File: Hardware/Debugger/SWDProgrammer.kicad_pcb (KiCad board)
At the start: 4 copper layers, 21.1 x 14 mm, 32 parts, among them J1 USB_C_Receptacle_USB2.0, U1 AP2112K-3.3, U2 STM32F103C8Tx, Y1 32.768KHZ, Y2 Crystal_GND24_Small

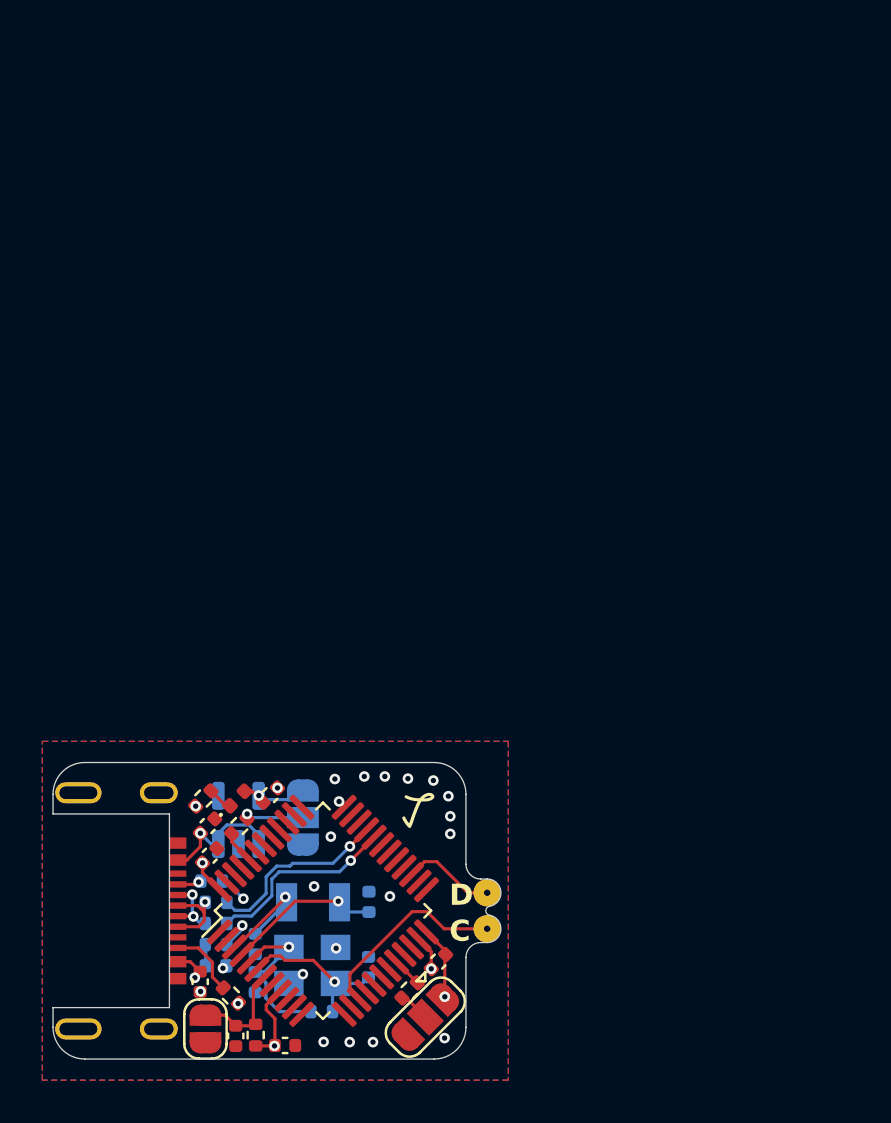
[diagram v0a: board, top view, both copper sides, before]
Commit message: worked on debugger, has to be flipped
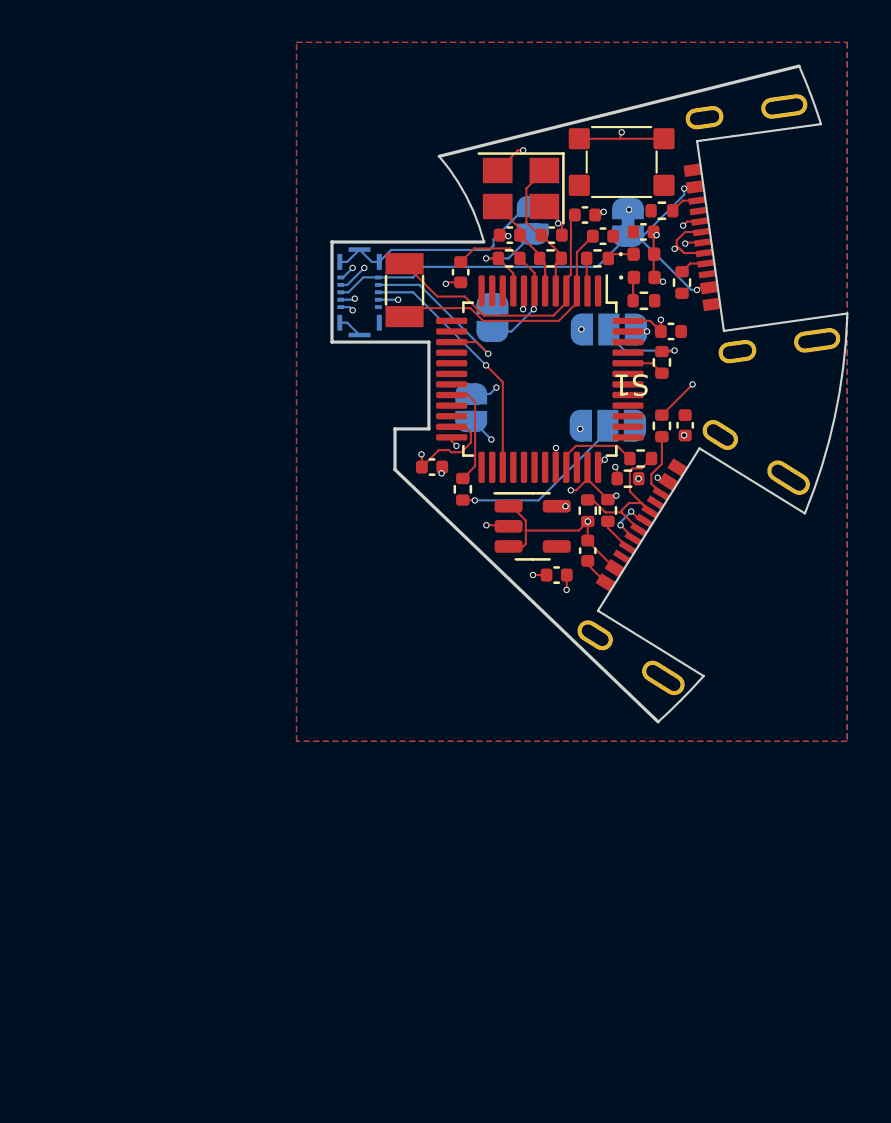
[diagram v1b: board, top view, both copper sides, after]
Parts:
- removed the JP1 at (126.7, 94.6)
- removed P1: ~, Library:Programmer Pin
- added J2: USB_C_Receptacle_USB2.0, Library:USB-C_C168688, F.Cu at (150.5, 57.2)
- added JP1: SolderJumper_2_Open, Jumper:SolderJumper-2_P1.3mm_Open_RoundedPad1.0x1.5mm, B.Cu at (140.2, 61.0)
- added JP1: SolderJumper_2_Open, Jumper:SolderJumper-2_P1.3mm_Open_RoundedPad1.0x1.5mm, B.Cu at (139.2, 65.2)
- added JP4: Jumper_2_Open, Jumper:SolderJumper-2_P1.3mm_Open_RoundedPad1.0x1.5mm, B.Cu at (142.2, 56.4)
- added JP5: Jumper_2_Bridged, Jumper:SolderJumper-2_P1.3mm_Bridged_RoundedPad1.0x1.5mm, B.Cu at (146.7, 56.5)
- added R11: 1.5K, Resistor_SMD:R_0402_1005Metric, F.Cu at (144.8, 70.1)
- added R12: 5.1K, Resistor_SMD:R_0402_1005Metric, F.Cu at (148.2, 56.0)
- added R13: 5.1K, Resistor_SMD:R_0402_1005Metric, F.Cu at (149.2, 59.3)
- added S1: Button, Library:button 3x3, F.Cu at (146.3, 53.6)
- added U3: ~, Library:BK13C06-10DS, B.Cu at (134.0, 59.8)
- C10, C11, C3, C4, D1, R10, R3, R5, R6, R7, U1, Y1: moved to F.Cu
- JP3: moved to B.Cu
- Y2: value Crystal_GND24_Small -> 8Mhz; moved to F.Cu
- moved D1 39.2 mm to (147.4, 58.0)
- moved R4 38.6 mm to (141.0, 58.2), turned to 0 degrees
- moved Y2 38.0 mm to (141.6, 54.9), turned to 180 degrees
- moved C11 37.9 mm to (143.1, 57.1), turned to 180 degrees
- moved C5 37.6 mm to (138.8, 58.9)
- moved C3 37.2 mm to (145.5, 57.1), turned to 180 degrees
- moved R7 37.2 mm to (143.0, 58.2), turned to 0 degrees
- moved R3 37.1 mm to (145.2, 58.2), turned to 180 degrees
- moved C7 35.9 mm to (147.4, 57.0), turned to 0 degrees
- moved C10 35.2 mm to (141.1, 57.1), turned to 0 degrees
- moved C4 34.0 mm to (144.6, 56.1), turned to 0 degrees
- moved R9 33.7 mm to (148.2, 66.1), turned to -90 degrees
- moved R8 31.4 mm to (147.4, 60.2), turned to 0 degrees
- moved D2 31.2 mm to (147.4, 59.1), turned to 0 degrees
- moved R1 29.6 mm to (148.2, 63.1), turned to -90 degrees
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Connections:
- J1 pad S2: unconnected-(J1-SHIELD-PadS1) -> unconnected-(J1-SHIELD-PadS2)
- J1 pad S3: unconnected-(J1-SHIELD-PadS1) -> unconnected-(J1-SHIELD-PadS3)
- J1 pad S4: unconnected-(J1-SHIELD-PadS1) -> unconnected-(J1-SHIELD-PadS4)
- U2 pad 15: /A5 -> swc
- U2 pad 27: /B14 -> swd
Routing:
- net 5V(2): track 0.00 -> 23.9 mm, vias 0 -> 2
- net D-: track 0.00 -> 20.7 mm, vias 0 -> 2
- net D+: track 0.00 -> 20.6 mm, vias 0 -> 3
- net RESET: track 0.00 -> 20.5 mm, vias 0 -> 2
- net GND: track 2.96 -> 21.6 mm, vias 23 -> 13
- net SDA: track 0.00 -> 14.1 mm, vias 0 -> 2
- net 5V: track 15.4 -> 28.8 mm, vias 2 -> 4
- net SCL: track 0.00 -> 12.6 mm, vias 0 -> 2
- net swd: track 0.00 -> 11.7 mm, vias 0 -> 1
- net VDD_nRF: track 0.00 -> 10.8 mm
- net /A5: track 9.42 -> 0.00 mm
- net swc: track 0.00 -> 8.49 mm, vias 0 -> 1
- net unconnected-(J1-SHIELD-PadS1): track 7.60 -> 0.00 mm
- net /BOOT1: track 1.47 -> 8.46 mm, vias 0 -> 1
- net Net-(U2-PC14): track 5.51 -> 12.4 mm, vias 1 -> 0
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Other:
- board size 21.1 x 14 mm -> 24.3 x 31 mm
- board text added: "3V"
- board text added: "5V"
- board text added: "BOOT0"
- board text added: "BOOT1"
- board text added: "PASS TO"
- board text added: "RST"
- board text added: "SCL"
- board text added: "SDA"
- board text removed: "Tongtong.inc"

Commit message: finished debugger and wireless
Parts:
- added JP7: SolderJumper_2_Open, Jumper:SolderJumper-2_P1.3mm_Open_RoundedPad1.0x1.5mm, F.Cu at (141.2, 62.5)
- added JP7: SolderJumper_2_Open, Jumper:SolderJumper-2_P1.3mm_Open_RoundedPad1.0x1.5mm, F.Cu at (141.2, 59.7)
- C1, C10, C11, C2, C3, C4, C5, C6, C7, C8, C9, D1, D2, J1, J2, R1, R10, R11, R12, R13, R2, R3, R4, R5, R6, R7, R8, R9, S1, U1, U2, Y1, Y2: moved to B.Cu
- JP1, JP2, JP3, JP4, JP5, U3: moved to F.Cu
- JP7: renamed from JP1; moved to F.Cu
- moved C8 12.2 mm to (138.7, 68.6), turned to 90 degrees
- moved C9 11.1 mm to (148.3, 66.2), turned to -90 degrees
- moved R2 10.9 mm to (148.8, 64.5), turned to 180 degrees
- moved R4 10.4 mm to (137.6, 68.0), turned to 90 degrees
- moved Y1 10.2 mm to (145.8, 56.6), turned to 0 degrees
- moved C7 10.1 mm to (137.8, 60.2)
- moved D1 9.79 mm to (137.7, 58.9), turned to -90 degrees
- moved JP1 8.23 mm to (140.9, 69.2), turned to 0 degrees
- moved R9 6.93 mm to (144.7, 72.1)
- moved R3 6.59 mm to (138.7, 58.9), turned to -90 degrees
- moved C6 4.76 mm to (139.6, 70.1), turned to 90 degrees
- moved C5 4.59 mm to (143.3, 58.2), turned to 180 degrees
- moved R12 3.87 mm to (149.2, 59.7), turned to 90 degrees
- moved R6 3.56 mm to (145.2, 70.6)
- moved R11 3.54 mm to (147.2, 67.6), turned to 180 degrees
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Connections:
- U2 pad 30: unconnected-(U2-PA9-Pad30) -> /A9
- U2 pad 31: unconnected-(U2-PA10-Pad31) -> /A10
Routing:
- net GND: track 21.6 -> 5.85 mm, vias 13 -> 6
- net 5V: track 28.8 -> 42.4 mm
- net Net-(JP1-A): track 8.35 -> 18.7 mm, vias 1 -> 2
- net Net-(U2-BOOT0): track 1.79 -> 10.8 mm, vias 0 -> 2
- net swc: track 8.49 -> 16.6 mm, vias 1 -> 2
- net 3.3V: track 12.7 -> 19.7 mm, vias 11 -> 6
- net /A9: track 0.00 -> 6.74 mm, vias 0 -> 1
- net /A10: track 0.00 -> 5.20 mm, vias 0 -> 1
- net SDA: track 14.1 -> 9.49 mm, vias 2 -> 0
- net swd: track 11.7 -> 16.2 mm, vias 1 -> 2
- net SCL: track 12.6 -> 8.22 mm, vias 2 -> 0
- net Net-(U2-PC15): track 13.2 -> 9.46 mm
- net Net-(U2-PB2): track 5.09 -> 1.63 mm
- net /BOOT1: track 8.46 -> 5.62 mm
- net /BOOT0: track 4.28 -> 6.30 mm
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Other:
- board text added: "5v"
- board text added: "DEBUGGER"
- board text added: "Gnd"
- board text added: "PASSTHROUGH"
- board text added: "Rx"
- board text added: "Tx"
- board text removed: "PASS TO"

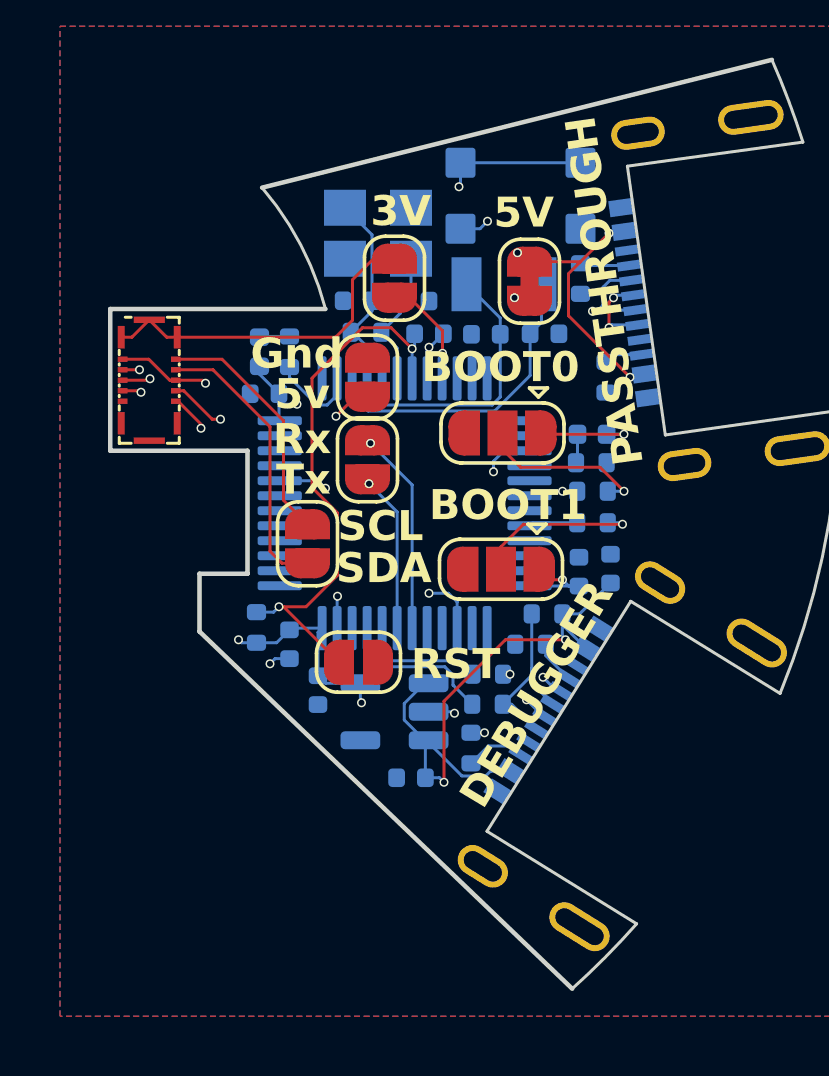
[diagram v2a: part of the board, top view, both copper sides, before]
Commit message: changed via hole sizes
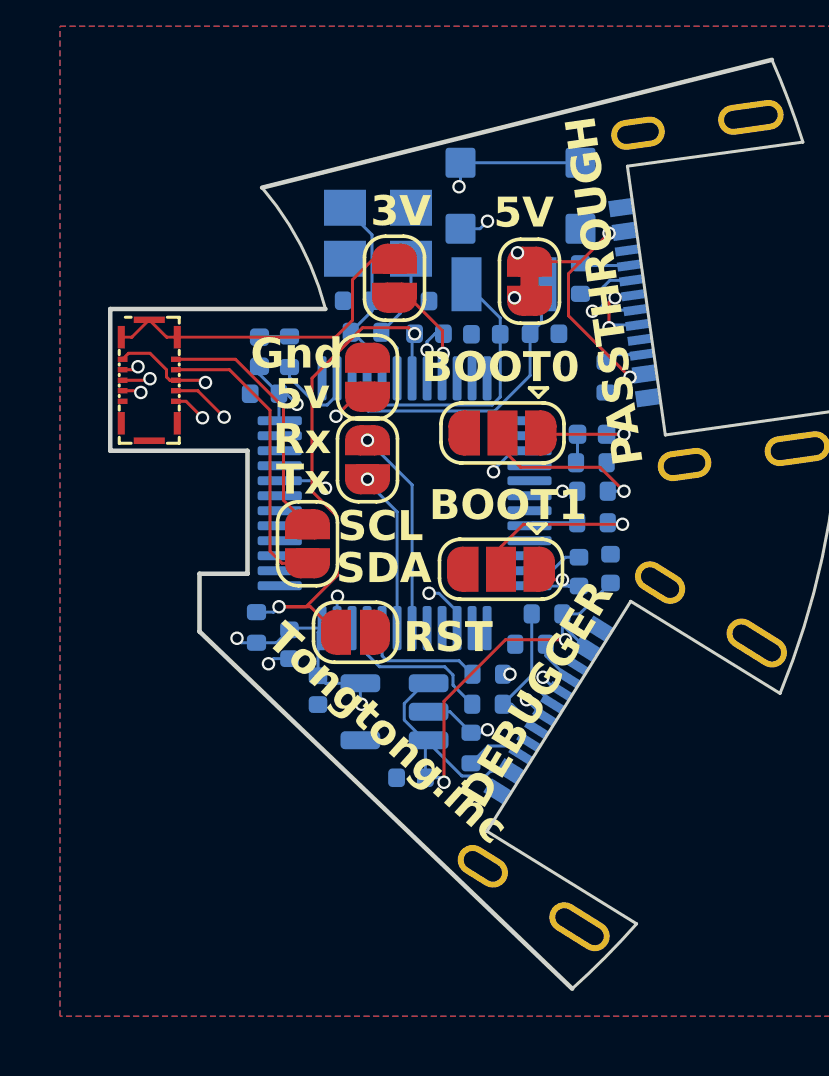
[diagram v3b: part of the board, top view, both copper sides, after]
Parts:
- moved JP1 1.00 mm to (140.8, 68.2)
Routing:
- net GND: track 5.85 -> 8.85 mm, vias 6 -> 5
- net Net-(JP1-A): track 18.7 -> 18.1 mm
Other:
- board text added: "Tongtong.inc"

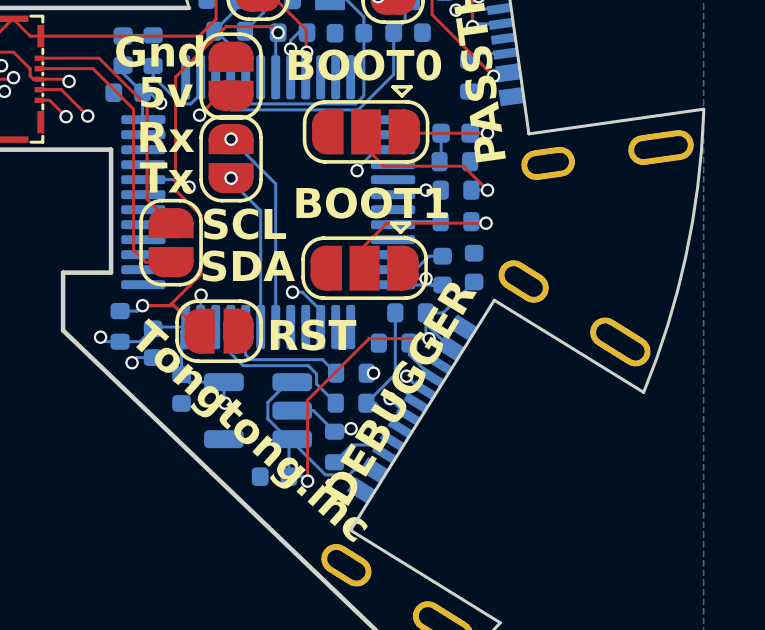
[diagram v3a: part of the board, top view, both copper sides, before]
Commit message: fixed problems on debugger
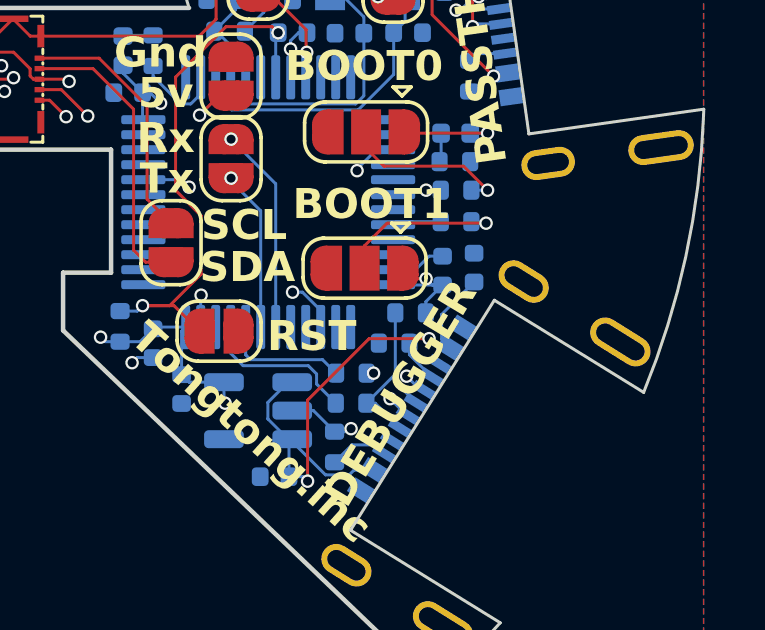
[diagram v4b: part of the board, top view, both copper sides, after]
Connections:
- R11 pad 1: 5V -> 3.3V
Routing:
- net 3.3V: track 20.0 -> 21.2 mm
- net 5V: track 42.4 -> 41.6 mm
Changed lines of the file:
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@@
       (stroke (width 0.1) (type solid)) (layer "B.Fab"))
     (pad "1" smd roundrect (at -0.51 0 180) (size 0.54 0.64) (layers "B.Cu" "B.Paste" "B.Mask") (roundrect_rratio 0.25)
-      (net 6 "5V") (pintype "passive"))
+      (net 4 "3.3V") (pintype "passive"))
     (pad "2" smd roundrect (at 0.51 0 180) (size 0.54 0.64) (layers "B.Cu" "B.Paste" "B.Mask") (roundrect_rratio 0.25)
       (net 9 "/USBDP") (pintype "passive"))
@@
     )
   )
+  (gr_line (start 146.35 52.4) (end 146.35 53.1)
+    (stroke (width 0.15) (type default)) (layer "B.SilkS"))
+  (gr_line (start 146.35 54.1) (end 146.35 54.95)
+    (stroke (width 0.15) (type default)) (layer "B.SilkS"))
+  (gr_line (start 146.35 53.1) (end 146.65 54)
+    (stroke (width 0.15) (type default)) (layer "B.SilkS"))
   (gr_line (start 149.912796 52.66442) (end 151.176938 61.624566)
     (stroke (width 0.1) (type default)) (layer "Edge.Cuts"))
@@
   (segment (start 139.85 69.9) (end 141.0125 69.9) (width 0.1) (layer "B.Cu") (net 4))
   (segment (start 137.55 68.550001) (end 138.219999 68.550001) (width 0.1) (layer "B.Cu") (net 4))
+  (segment (start 147.744721 67.215279) (end 148.3 66.66) (width 0.1) (layer "B.Cu") (net 4))
   (segment (start 137.65 59.6) (end 138.3 60.25) (width 0.1) (layer "B.Cu") (net 4))
   (segment (start 141.0125 70.5625) (end 141.05 70.6) (width 0.1) (layer "B.Cu") (net 4))
@@
   (segment (start 139.6 69.65) (end 139.6 68.2) (width 0.1) (layer "B.Cu") (net 4))
   (segment (start 148.3 66.66) (end 146.66 66.66) (width 0.1) (layer "B.Cu") (net 4))
+  (segment (start 147.744721 67.588413) (end 147.744721 67.215279) (width 0.1) (layer "B.Cu") (net 4))
   (segment (start 143.7375 58.938748) (end 143.771839 58.904409) (width 0.1) (layer "B.Cu") (net 4))
   (segment (start 138.55 60.25) (end 138.9 60.6) (width 0.1) (layer "B.Cu") (net 4))
@@
   (segment (start 148.8 67.5) (end 148.8 59.7) (width 0.1) (layer "In2.Cu") (net 6))
   (segment (start 143.18 73.05) (end 143.65 73.05) (width 0.1) (layer "B.Cu") (net 6))
-  (segment (start 147.744721 67.588413) (end 147.744721 68.344721) (width 0.1) (layer "B.Cu") (net 6))
+  (segment (start 148.266954 67.643046) (end 149.35 66.56) (width 0.1) (layer "B.Cu") (net 6))
   (segment (start 143.150736 71.8) (end 142.475 71.124264) (width 0.1) (layer "B.Cu") (net 6))
-  (segment (start 147.744721 68.344721) (end 147.85 68.45) (width 0.1) (layer "B.Cu") (net 6))
+  (segment (start 148.266954 68.471074) (end 148.266954 67.643046) (width 0.1) (layer "B.Cu") (net 6))
   (segment (start 143.150736 69.9) (end 143.2875 69.9) (width 0.1) (layer "B.Cu") (net 6))
+  (segment (start 148.557237 68.761357) (end 148.266954 68.471074) (width 0.1) (layer "B.Cu") (net 6))
+  (segment (start 148.161357 68.761357) (end 147.85 68.45) (width 0.1) (layer "B.Cu") (net 6))
   (segment (start 145.190095 72.990095) (end 145.348202 72.831988) (width 0.1) (layer "B.Cu") (net 6))
-  (segment (start 147.744721 67.588413) (end 148.321587 67.588413) (width 0.1) (layer "B.Cu") (net 6))
   (segment (start 144.397044 72.990095) (end 145.190095 72.990095) (width 0.1) (layer "B.Cu") (net 6))
   (segment (start 143.65 73.05) (end 143.8 73.2) (width 0.1) (layer "B.Cu") (net 6))
   (segment (start 142.475 71.124264) (end 142.475 70.575736) (width 0.1) (layer "B.Cu") (net 6))
+  (segment (start 148.557237 68.761357) (end 148.161357 68.761357) (width 0.1) (layer "B.Cu") (net 6))
   (segment (start 143.18 73.05) (end 143.18 71.9075) (width 0.1) (layer "B.Cu") (net 6))
   (segment (start 143.2875 71.8) (end 143.150736 71.8) (width 0.1) (layer "B.Cu") (net 6))
   (segment (start 143.2875 71.880551) (end 144.397044 72.990095) (width 0.1) (layer "B.Cu") (net 6))
-  (segment (start 147.744721 67.588413) (end 147.744721 67.948841) (width 0.1) (layer "B.Cu") (net 6))
-  (segment (start 148.321587 67.588413) (end 149.35 66.56) (width 0.1) (layer "B.Cu") (net 6))
   (segment (start 145.348202 72.831988) (end 146.013625 72.831988) (width 0.1) (layer "B.Cu") (net 6))
   (segment (start 142.475 70.575736) (end 143.150736 69.9) (width 0.1) (layer "B.Cu") (net 6))
   (segment (start 143.18 71.9075) (end 143.2875 71.8) (width 0.1) (layer "B.Cu") (net 6))
-  (segment (start 147.744721 67.948841) (end 148.557237 68.761357) (width 0.1) (layer "B.Cu") (net 6))
   (segment (start 143.2875 71.8) (end 143.2875 71.880551) (width 0.1) (layer "B.Cu") (net 6))
   (segment (start 148.25 61.6) (end 148.25 62.499999) (width 0.1) (layer "B.Cu") (net 7))
